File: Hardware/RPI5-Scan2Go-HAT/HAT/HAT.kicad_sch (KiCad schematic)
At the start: 3 parts, among them J1 RPi_GPIO, J2 RPi_GPIO, U1 Pico

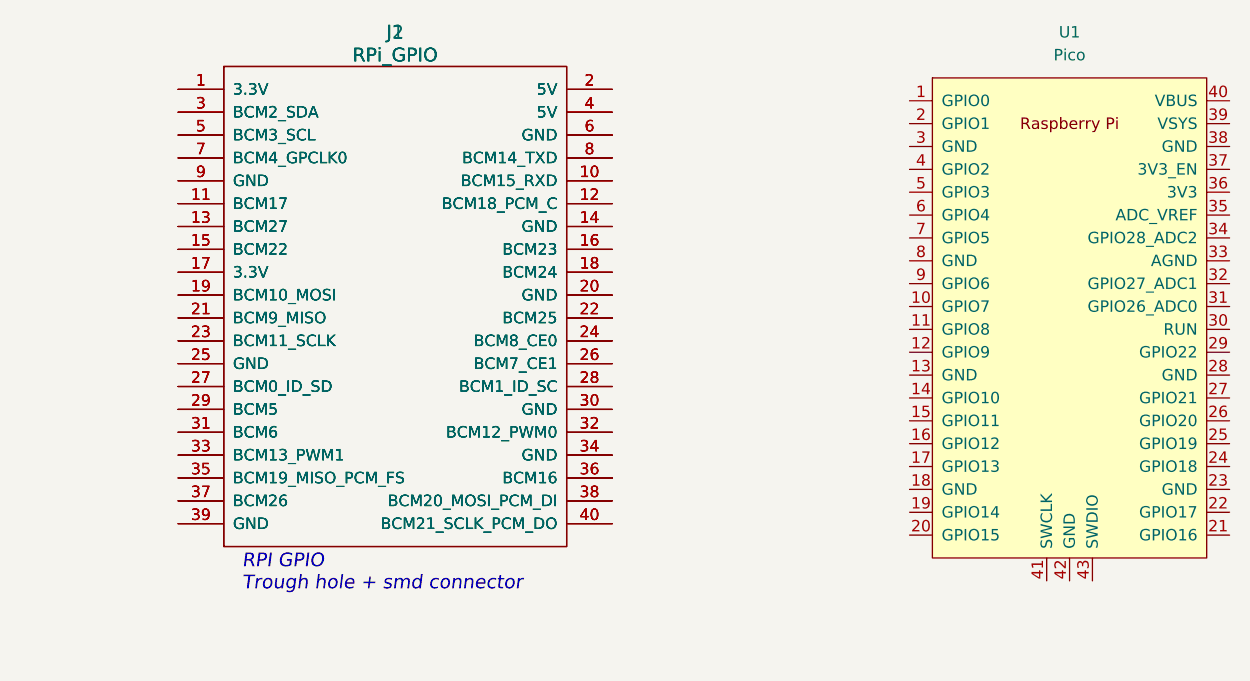
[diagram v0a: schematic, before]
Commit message: improved symbols of pico and rpi
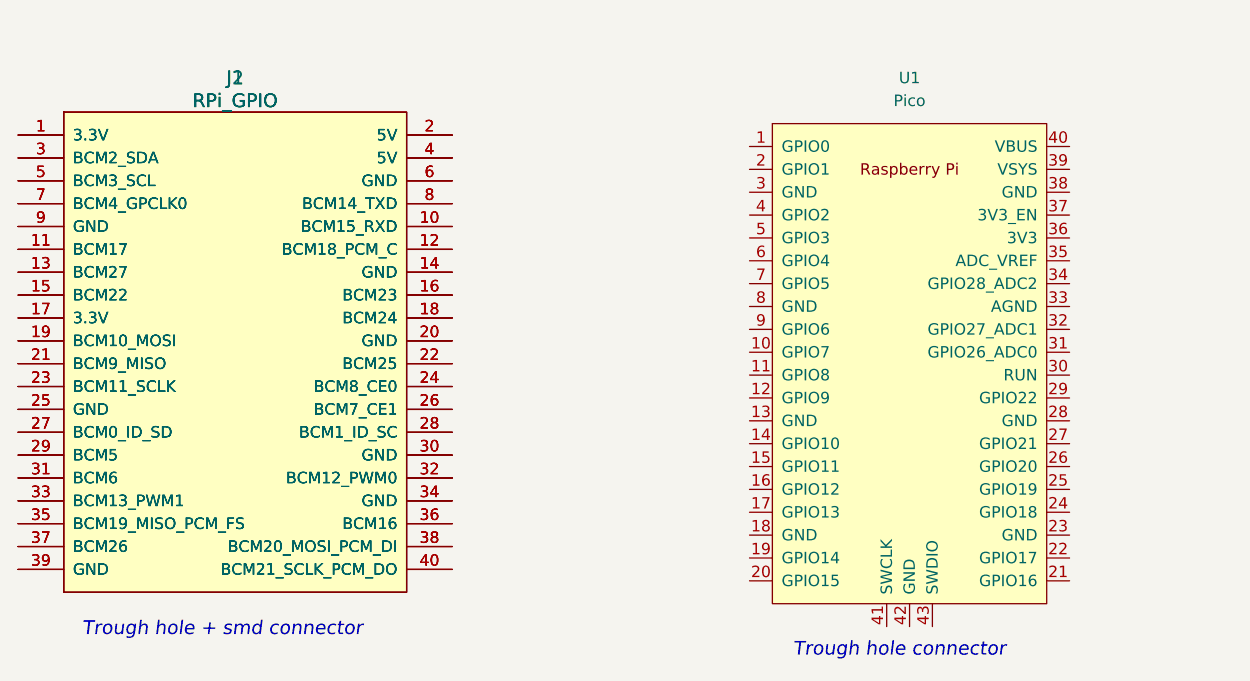
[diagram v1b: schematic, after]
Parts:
- U1: footprint RPi_Pico:RPi_Pico_SMD_TH -> MCU_RaspberryPi_and_Boards:RPi_Pico_SMD_TH
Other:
- note added: "Trough hole + smd connector"
- note added: "Trough hole connector"
- note removed: "RPI GPIO Trough hole + smd connector"
- moved on the sheet: J2, U1
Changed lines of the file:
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@@
 	(generator_version "8.0")
 	(paper "A4")
-	(text "RPI GPIO \nTrough hole + smd connector\n"
-		(exclude_from_sim no)
-		(at 129.032 115.57 0)
+	(text "Trough hole connector"
+		(exclude_from_sim no)
+		(at 190.246 122.936 0)
 		(effects
 			(font
@@
 		)
 	)
+	(text "Trough hole + smd connector\n"
+		(exclude_from_sim no)
+		(at 111.252 120.65 0)
+		(effects
+			(font
+				(size 1.524 1.524)
+				(italic yes)
+			)
+			(justify left bottom)
+		)
+	)
 	(symbol
 		(lib_id "RPi_Hat:RPi_GPIO")
-		(at 127 59.69 0)
+		(at 109.22 64.77 0)
 		(unit 1)
 		(exclude_from_sim no)
@@
 		(dnp no)
 		(property "Reference" "J2"
-			(at 146.05 53.34 0)
+			(at 128.27 58.42 0)
 			(effects
 				(font
@@
 		)
 		(property "Value" "RPi_GPIO"
-			(at 146.05 55.88 0)
+			(at 128.27 60.96 0)
 			(effects
 				(font
@@
 		)
 		(property "Footprint" "_custom:Samtec_HLE-120-02-XXX-DV-BE-XX-XX"
-			(at 127 59.69 0)
+			(at 109.22 64.77 0)
 			(effects
 				(font
@@
 		)
 		(property "Datasheet" ""
-			(at 127 59.69 0)
+			(at 109.22 64.77 0)
 			(effects
 				(font
@@
 		)
 		(property "Description" ""
-			(at 127 59.69 0)
+			(at 109.22 64.77 0)
 			(effects
 				(font
@@
 	)
 	(symbol
+		(lib_name "RPi_GPIO_1")
 		(lib_id "RPi_Hat:RPi_GPIO")
-		(at 127 59.69 0)
+		(at 109.22 64.77 0)
 		(unit 1)
 		(exclude_from_sim no)
@@
 		(dnp no)
 		(property "Reference" "J1"
-			(at 146.05 53.34 0)
+			(at 128.27 58.42 0)
 			(effects
 				(font
@@
 		)
 		(property "Value" "RPi_GPIO"
-			(at 146.05 55.88 0)
+			(at 128.27 60.96 0)
 			(effects
 				(font
@@
 		)
 		(property "Footprint" "_custom:Pin_Header_Straight_2x20"
-			(at 127 59.69 0)
+			(at 109.22 64.77 0)
 			(effects
 				(font
@@
 		)
 		(property "Datasheet" ""
-			(at 127 59.69 0)
+			(at 109.22 64.77 0)
 			(effects
 				(font
@@
 		)
 		(property "Description" ""
-			(at 127 59.69 0)
+			(at 109.22 64.77 0)
 			(effects
 				(font
@@
 	(symbol
 		(lib_id "MCU_RaspberryPi_and_Boards:Pico")
-		(at 220.98 85.09 0)
+		(at 203.2 90.17 0)
 		(unit 1)
 		(exclude_from_sim no)
@@
 		(fields_autoplaced yes)
 		(property "Reference" "U1"
-			(at 220.98 53.34 0)
+			(at 203.2 58.42 0)
 			(effects
 				(font
@@
 		)
 		(property "Value" "Pico"
-			(at 220.98 55.88 0)
-			(effects
-				(font
-					(size 1.27 1.27)
-				)
-			)
-		)
-		(property "Footprint" "RPi_Pico:RPi_Pico_SMD_TH"
-			(at 220.98 85.09 90)
+			(at 203.2 60.96 0)
+			(effects
+				(font
+					(size 1.27 1.27)
+				)
+			)
+		)
+		(property "Footprint" "MCU_RaspberryPi_and_Boards:RPi_Pico_SMD_TH"
+			(at 203.2 90.17 90)
 			(effects
 				(font
@@
 		)
 		(property "Datasheet" ""
-			(at 220.98 85.09 0)
+			(at 203.2 90.17 0)
 			(effects
 				(font
@@
 		)
 		(property "Description" ""
-			(at 220.98 85.09 0)
-			(effects
-				(font
+			(at 203.2 90.17 0)
+			(effects
+				(font

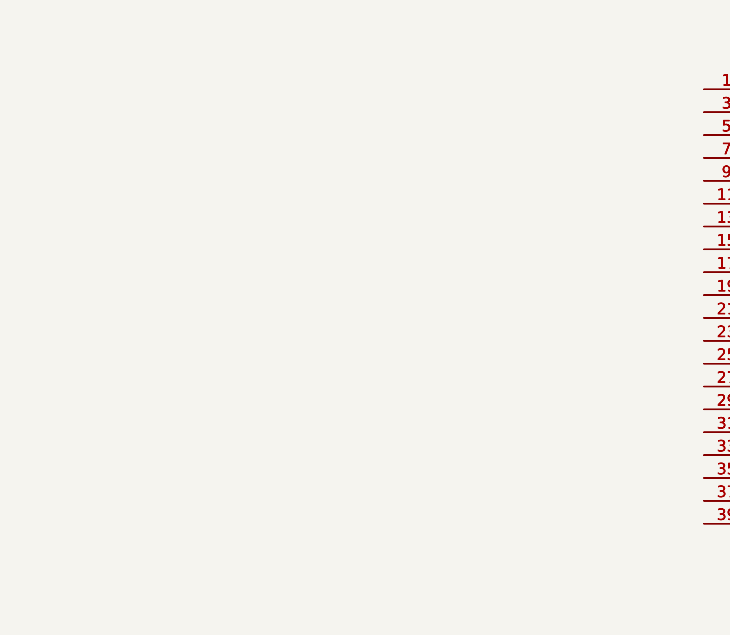
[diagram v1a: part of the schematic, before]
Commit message: created footprint for Adafruit amplifier
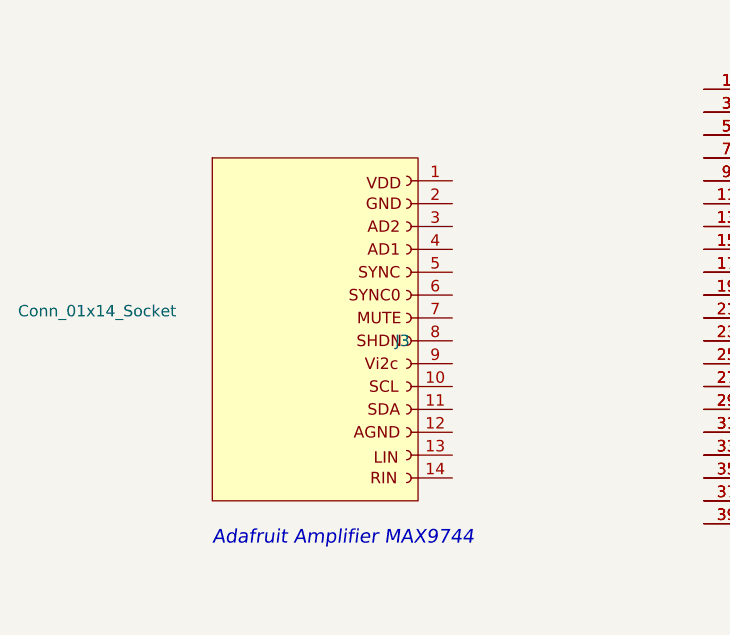
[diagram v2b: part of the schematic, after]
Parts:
- added J3: Conn_01x14_Socket, Connector_PinSocket_2.54mm:PinSocket_1x14_P2.54mm_Vertical, symbol Connector:Conn_01x14_Socket
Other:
- note added: "Adafruit Amplifier MAX9744"
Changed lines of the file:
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@@
 	(generator_version "8.0")
 	(paper "A4")
+	(text "Adafruit Amplifier MAX9744 "
+		(exclude_from_sim no)
+		(at 49.53 115.57 0)
+		(effects
+			(font
+				(size 1.524 1.524)
+				(italic yes)
+			)
+			(justify left bottom)
+		)
+	)
 	(text "Trough hole connector"
 		(exclude_from_sim no)
@@
 					(unit 1)
 				)
+			)
+		)
+	)
+	(symbol
+		(lib_id "Connector:Conn_01x14_Socket")
+		(at 40.64 88.9 0)
+		(unit 1)
+		(exclude_from_sim no)
+		(in_bom yes)
+		(on_board yes)
+		(dnp no)
+		(property "Reference" "J3"
+			(at 69.85 92.7099 0)
+			(effects
+				(font
+					(size 1.27 1.27)
+				)
+				(justify left)
+			)
+		)
+		(property "Value" "Conn_01x14_Socket"
+			(at 27.94 89.408 0)
+			(effects
+				(font
+					(size 1.27 1.27)
+				)
+				(justify left)
+			)
+		)
+		(property "Footprint" "Connector_PinSocket_2.54mm:PinSocket_1x14_P2.54mm_Vertical"
+			(at 71.12 90.17 0)
+			(effects
+				(font
+					(size 1.27 1.27)
+				)
+				(hide yes)
+			)
+		)
+		(property "Datasheet" "~"
+			(at 71.12 90.17 0)
+			(effects
+				(font
+					(size 1.27 1.27)
+				)
+				(hide yes)
+			)
+		)
+		(property "Description" "Generic connector, single row, 01x14, script generated"
+			(at 71.12 90.17 0)
+			(effects
+				(font
+					(size 1.27 1.27)
+				)
+				(hide yes)
+			)
+		)
+		(pin "12"
+		)
+		(pin "14"
+		)
+		(pin "9"
+		)
+		(pin "13"
+		)
+		(pin "8"
+		)
+		(pin "7"
+		)
+		(pin "2"
+		)
+		(pin "1"
+		)
+		(pin "10"
+		)
+		(pin "3"
+		)
+		(pin "11"
+		)
+		(pin "4"
+		)
+		(pin "6"
+		)
+		(pin "5"
+		)
+		(instances
+			(project "HAT"
+				(path "/3ab4cced-3a91-405a-aea0-e8513537e898"
+					(reference "J3")
+					(unit 1)
+				)

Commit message: started pcb routing
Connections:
- net GND: now reaches J1.6 (GND), J2.6 (GND)
- net GND: now also J3.2 (GND)
- net at J3.1 (VDD): now also U1.40 (VBUS)

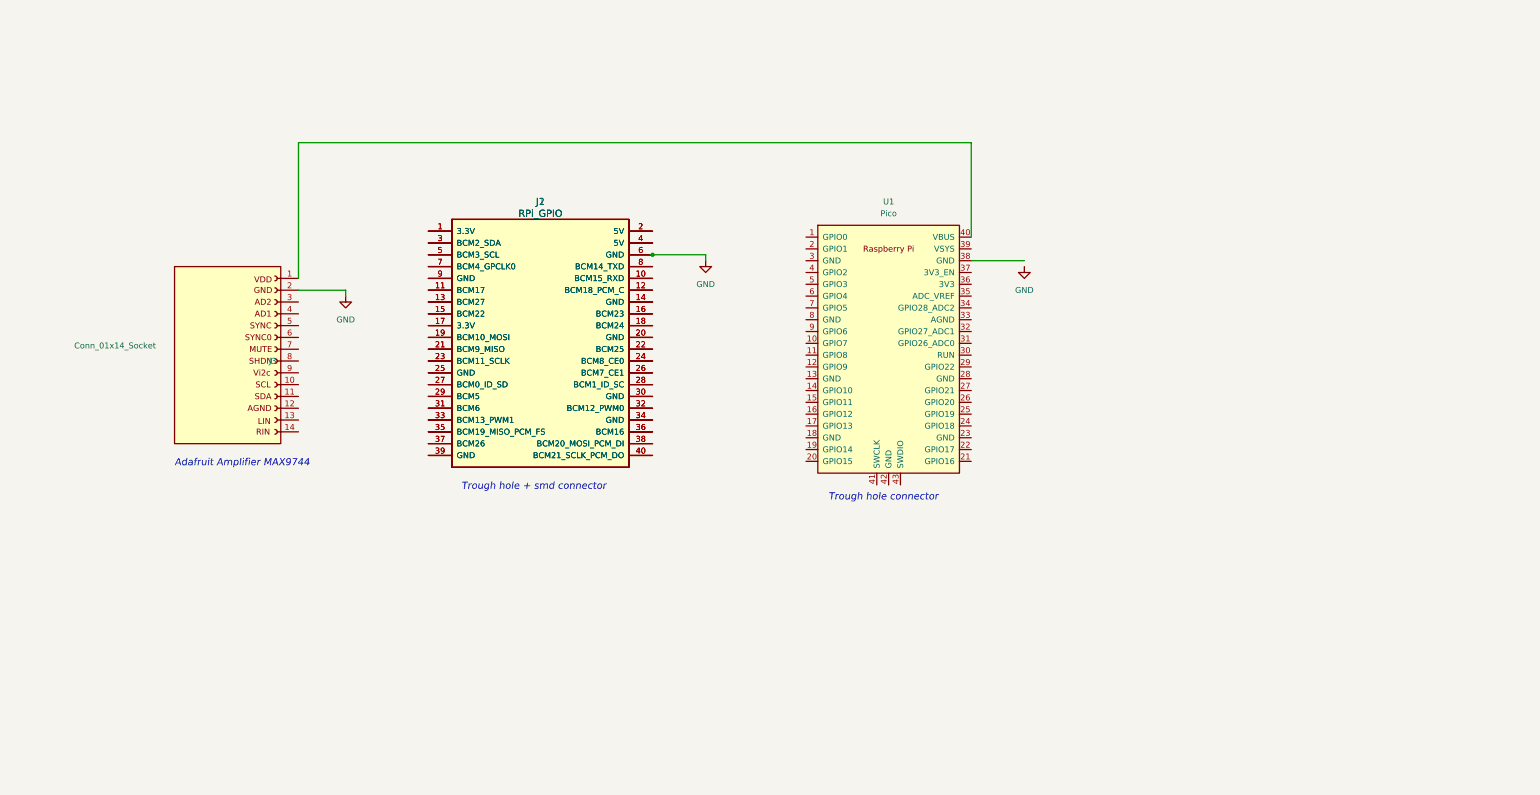
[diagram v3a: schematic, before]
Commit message: added power circuit and improved documentation
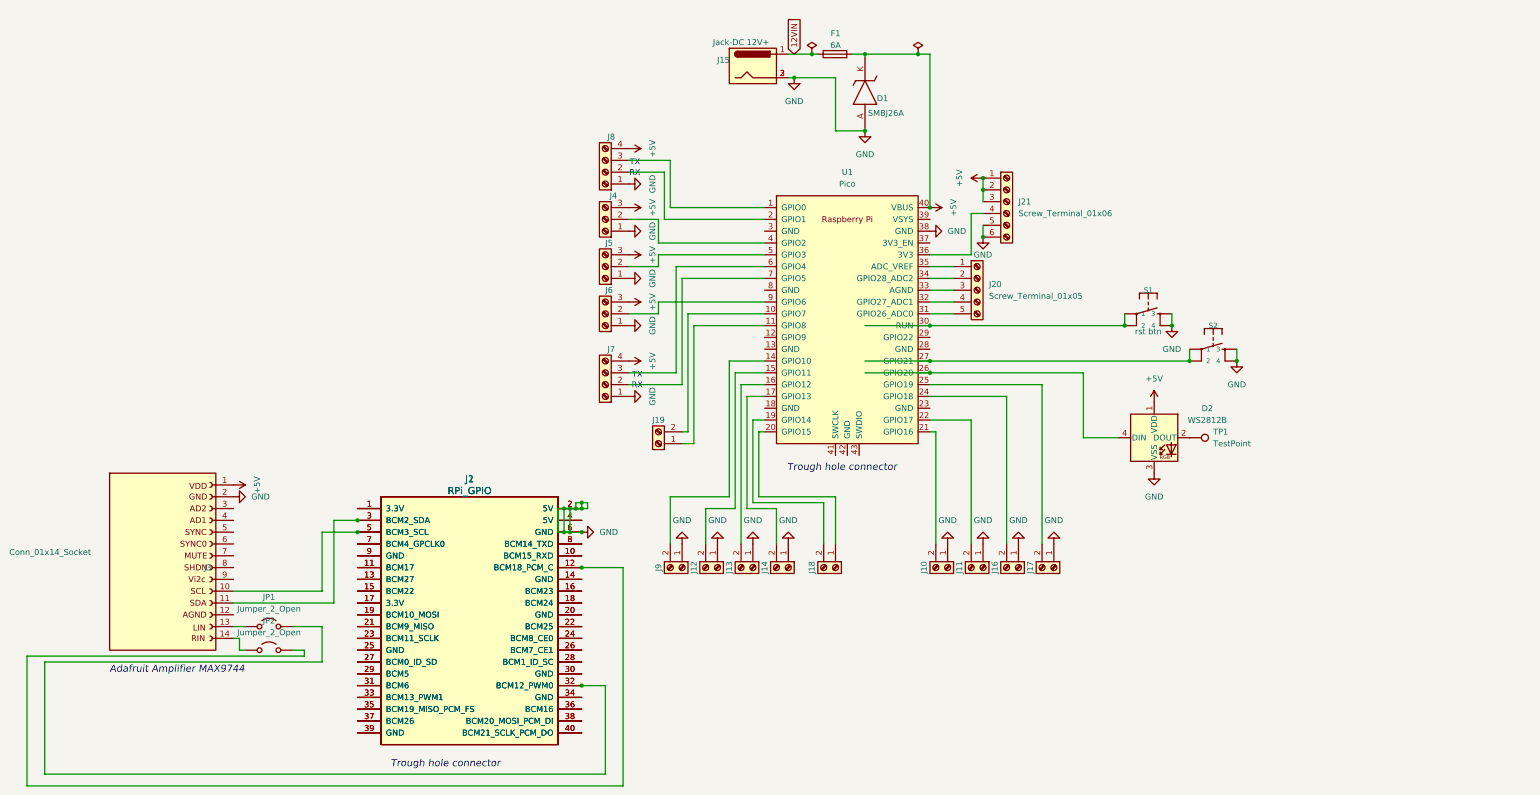
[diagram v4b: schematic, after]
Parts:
- added D1: SMBJ26A, SamacSys_Parts:DIOM5436X261N, symbol SamacSys_Parts:SMBJ26A
- added D2: WS2812B, LED_SMD:LED_WS2812B_PLCC4_5.0x5.0mm_P3.2mm, symbol LED:WS2812B
- added F1: 6A, Fuse:Fuse_2010_5025Metric_Pad1.52x2.65mm_HandSolder, symbol Device:Fuse
- added J10, J11, J12, J13, J14, J16, J17, J18, J19, J9: Screw_Terminal_01x02, symbol Connector:Screw_Terminal_01x02
- added J15: Jack-DC 12V+, Connector_BarrelJack:BarrelJack_Wuerth_6941xx301002, symbol Connector:Jack-DC
- added J20: Screw_Terminal_01x05, symbol Connector:Screw_Terminal_01x05
- added J21: Screw_Terminal_01x06, symbol Connector:Screw_Terminal_01x06
- added J4, J5, J6: Screw_Terminal_01x03, symbol Connector:Screw_Terminal_01x03
- added J7, J8: Screw_Terminal_01x04, symbol Connector:Screw_Terminal_01x04
- added JP1, JP2: Jumper_2_Open, symbol Jumper:Jumper_2_Open
- added S1, S2: MOMENTARY-SWITCH-SPST-2-SMD-5.2MM, Button_Switch_SMD:SW_SPST_TL3305B, symbol SparkFun-Switches:MOMENTARY-SWITCH-SPST-2-SMD-5.2MM
- added TP1: TestPoint, symbol Connector:TestPoint
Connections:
- net GND: now also J1.2 (5V), J2.2 (5V), U1.38 (GND), D1.A, D2.3 (VSS), J10.1 (Pin_1), J11.1 (Pin_1), J12.1 (Pin_1), J13.1 (Pin_1), J14.1 (Pin_1), J15.2, J15.3, J16.1 (Pin_1), J17.1 (Pin_1), J21.5 (Pin_5), J21.6 (Pin_6), J4.1 (Pin_1), J5.1 (Pin_1), J6.1 (Pin_1), J7.1 (Pin_1), J8.1 (Pin_1), J9.1 (Pin_1), S1.3, S1.4, S2.3, S2.4
- net at J1.12 (BCM18_PCM_C), J2.12 (BCM18_PCM_C): now also JP2.2 (B)
- net at J1.3 (BCM2_SDA), J2.3 (BCM2_SDA): now also J3.11 (SDA)
- net at J1.32 (BCM12_PWM0), J2.32 (BCM12_PWM0): now also JP1.2 (B)
- net at J1.5 (BCM3_SCL), J2.5 (BCM3_SCL): now also J3.10 (SCL)
- net +5V: now reaches J3.1 (VDD), U1.40 (VBUS)
- net +5V: now also D1.K, D2.1 (VDD), F1.2, J21.1 (Pin_1), J21.2 (Pin_2), J21.3 (Pin_3), J4.3 (Pin_3), J5.3 (Pin_3), J6.3 (Pin_3), J7.4 (Pin_4), J8.4 (Pin_4)
- net at J3.13 (LIN): now also JP1.1 (A)
- net at J3.14 (RIN): now also JP2.1 (A)
- net at U1.1 (GPIO0): now also J8.3 (Pin_3)
- net at U1.10 (GPIO7): now also J19.2 (Pin_2)
- net at U1.11 (GPIO8): now also J19.1 (Pin_1)
- net at U1.14 (GPIO10): now also J9.2 (Pin_2)
- net at U1.15 (GPIO11): now also J12.2 (Pin_2)
- net at U1.16 (GPIO12): now also J13.2 (Pin_2)
- net at U1.17 (GPIO13): now also J14.2 (Pin_2)
- net at U1.19 (GPIO14): now also J18.2 (Pin_2)
- net at U1.2 (GPIO1): now also J8.2 (Pin_2)
- net at U1.20 (GPIO15): now also J18.1 (Pin_1)
- net at U1.21 (GPIO16): now also J10.2 (Pin_2)
- net at U1.22 (GPIO17): now also J11.2 (Pin_2)
- net at U1.24 (GPIO18): now also J16.2 (Pin_2)
- net at U1.25 (GPIO19): now also J17.2 (Pin_2)
- net at U1.26 (GPIO20): now also D2.4 (DIN)
- net at U1.27 (GPIO21): now also S2.1, S2.2
- net at U1.30 (RUN): now also S1.1, S1.2
- net at U1.31 (GPIO26_ADC0): now also J20.5 (Pin_5)
- net at U1.32 (GPIO27_ADC1): now also J20.4 (Pin_4)
- net at U1.33 (AGND): now also J20.3 (Pin_3)
- net at U1.34 (GPIO28_ADC2): now also J20.2 (Pin_2)
- net at U1.35 (ADC_VREF): now also J20.1 (Pin_1)
- net at U1.36 (3V3): now also J21.4 (Pin_4)
- net at U1.4 (GPIO2): now also J4.2 (Pin_2)
- net at U1.5 (GPIO3): now also J5.2 (Pin_2)
- net at U1.6 (GPIO4): now also J7.3 (Pin_3)
- net at U1.7 (GPIO5): now also J7.2 (Pin_2)
- net at U1.9 (GPIO6): now also J6.2 (Pin_2)
- new net: D2.2 (DOUT), TP1.1
- new net 12VIN: F1.1, J15.1
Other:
- note added: "RX"
- note added: "TX"
- note removed: "Trough hole + smd connector"
- company: (none) -> Casper R. Tak
- title: (none) -> Scan2Go RPI-HAT
- moved on the sheet: J1, J2, J3, U1

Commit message: schematic finished for now (to be reviewed)
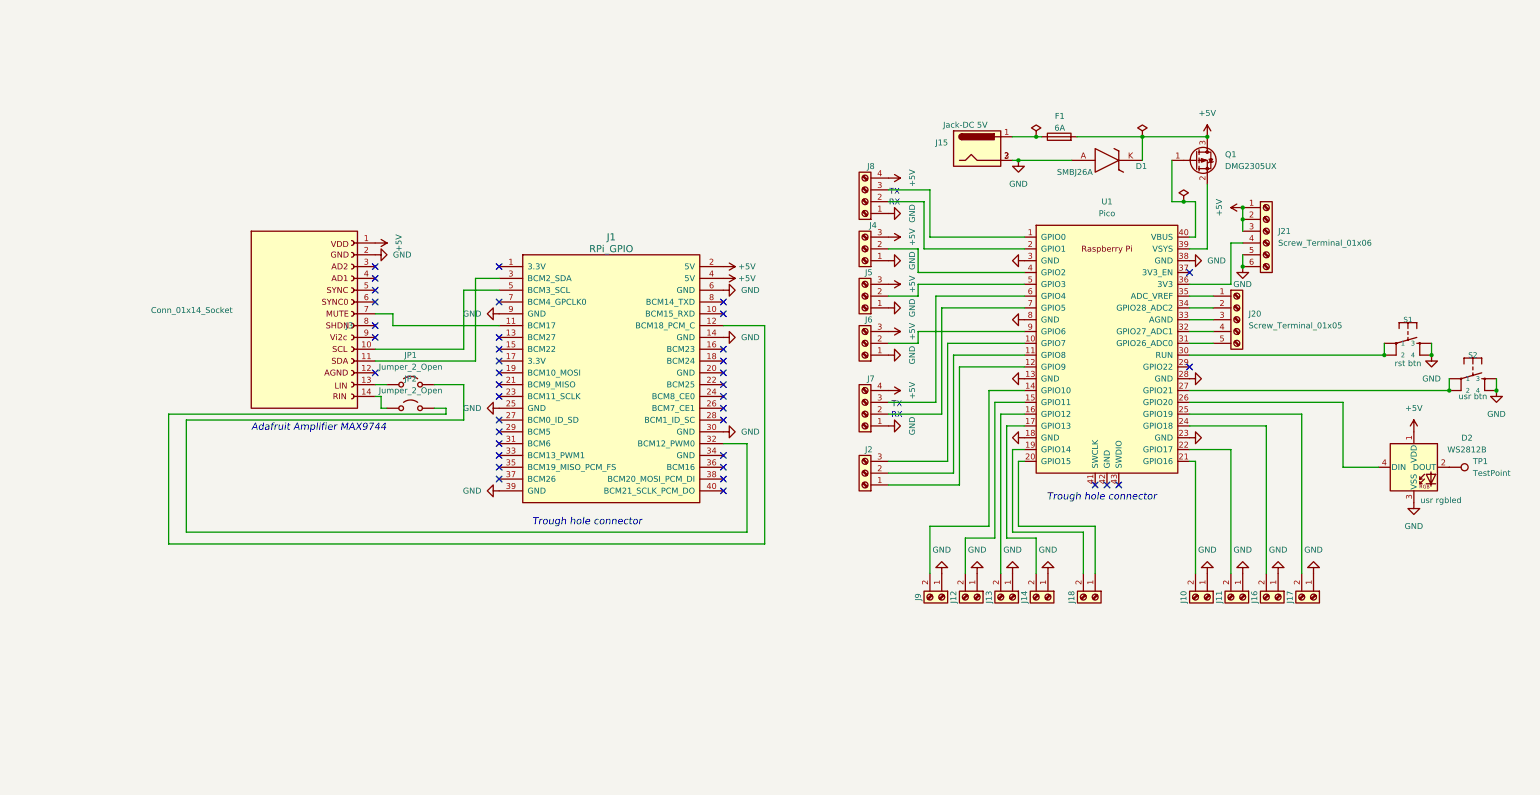
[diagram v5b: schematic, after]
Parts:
- removed J19: Screw_Terminal_01x02, symbol Connector:Screw_Terminal_01x02
- removed J2: RPi_GPIO, _custom:Samtec_HLE-120-02-XXX-DV-BE-XX-XX, symbol RPi_Hat:RPi_GPIO
- added J2: Screw_Terminal_01x03, symbol Connector:Screw_Terminal_01x03
- added Q1: DMG2305UX, Package_TO_SOT_SMD:SOT-23, symbol Transistor_FET:DMG2301L
- D2: Purpose (none) -> usr rgbled
- J15: value Jack-DC 12V+ -> Jack-DC 5V
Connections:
- net +5V: now also J1.2 (5V), J1.4 (5V), Q1.3 (D); no longer U1.40 (VBUS)
- net GND: now also J1.14 (GND), J1.25 (GND), J1.30 (GND), J1.39 (GND), J1.9 (GND), U1.13 (GND), U1.18 (GND), U1.23 (GND), U1.28 (GND), U1.3 (GND), U1.8 (GND); no longer J1.2 (5V)
- net at U1.11 (GPIO8): now also J2.2 (Pin_2)
- net at U1.10 (GPIO7): now also J2.3 (Pin_3)
- net at J1.11 (BCM17): now also J3.7 (MUTE)
- net at U1.12 (GPIO9): now also J2.1 (Pin_1)
- net at U1.39 (VSYS): now also Q1.2 (S)
- net 12VIN: no longer names the net of F1.1, J15.1
- new net: Q1.1 (G), U1.40 (VBUS)
- no-connect marks 0 -> 39
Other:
- moved on the sheet: D1, D2, F1, J1, J10, J11, J12, J13, J14, J15, J16, J17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
